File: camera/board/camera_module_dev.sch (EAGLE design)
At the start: 55 parts, among them IC1 74541PW, IC2 74541PW, Q1 MOSFET-NCHANNELBSS123LT1G, Q2 MOSFET-NCHANNELBSS123LT1G

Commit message: Fixed spacing for TCM camera pads, updated pullup resitor val on reset line
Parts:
- R5: value 10k -> 1k
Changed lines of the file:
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@@
 <part name="GND2" library="supply1" deviceset="GND" device=""/>
 <part name="GND3" library="supply1" deviceset="GND" device=""/>
-<part name="R5" library="biomimetic" deviceset="RESISTOR" device="0402-RES" value="10k"/>
+<part name="R5" library="biomimetic" deviceset="RESISTOR" device="0402-RES" value="1k"/>
 <part name="GND4" library="supply1" deviceset="GND" device=""/>
 <part name="GND5" library="supply1" deviceset="GND" device=""/>

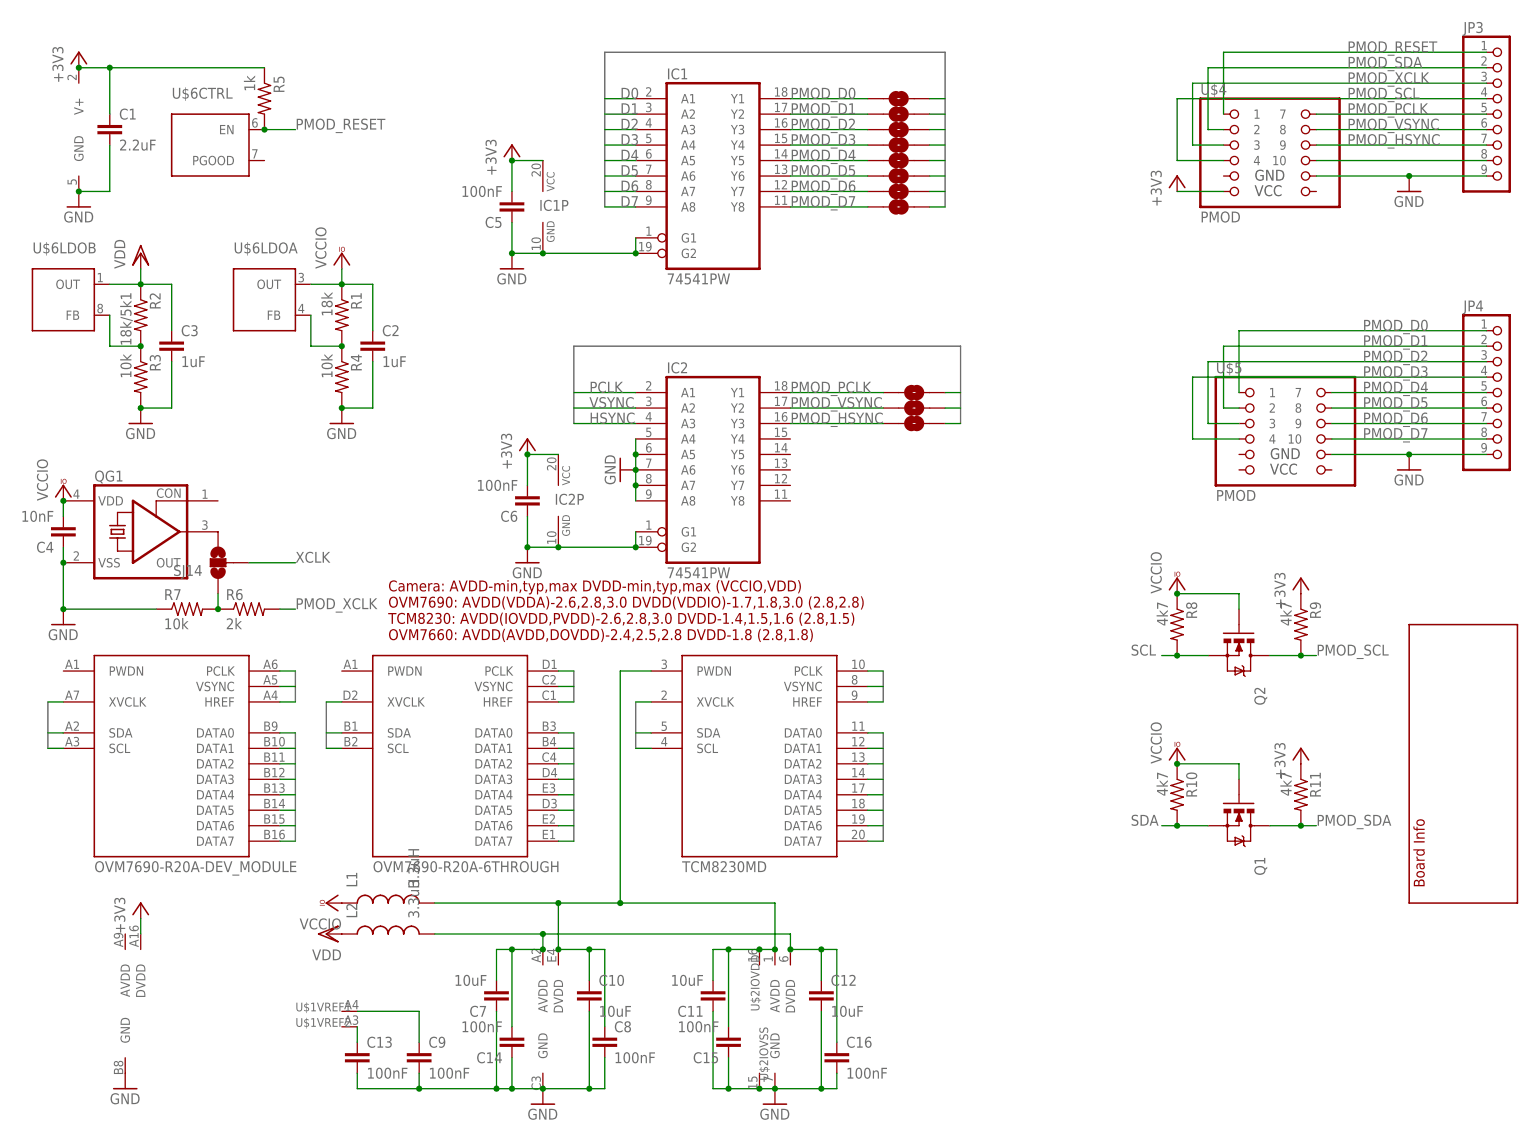
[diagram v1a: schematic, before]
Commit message: Laying out smaller TCM camera board
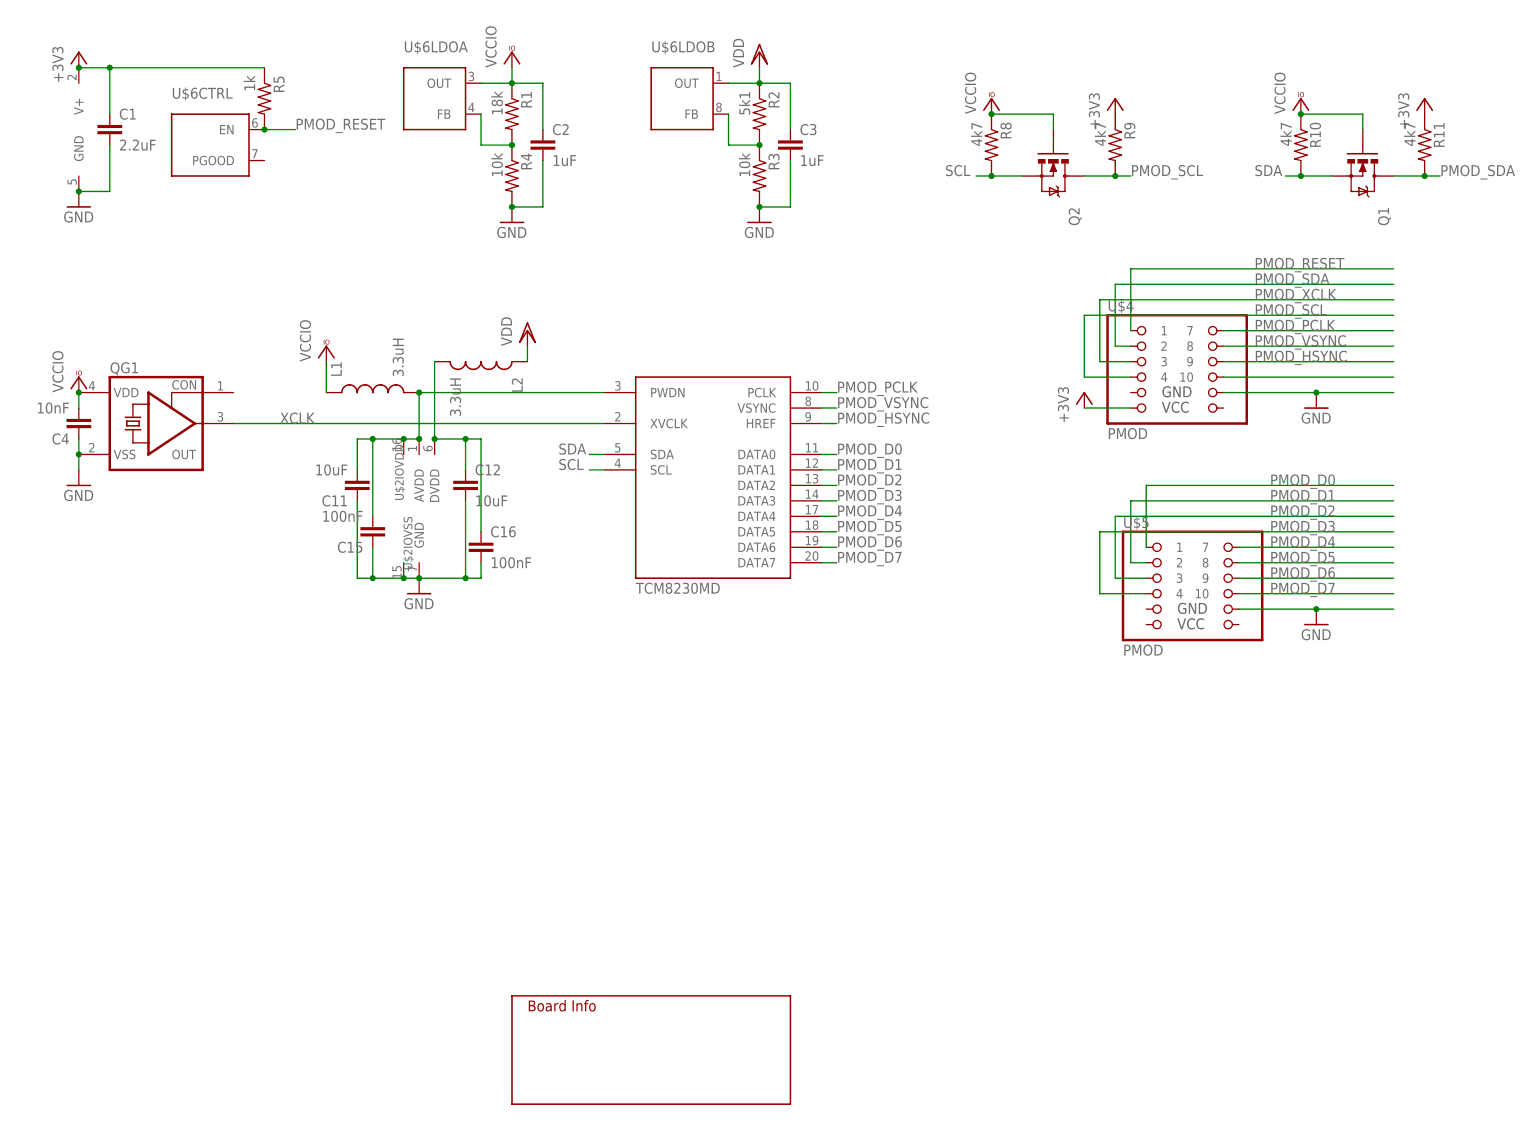
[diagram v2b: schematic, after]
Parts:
- removed C10, C7: 10uF, biomimetic:CAP0603-CAP
- removed C13, C14, C5, C6, C8, C9: 100nF, biomimetic:CAP0402-CAP
- removed IC1, IC2: 74541PW, modular_robotics:74541PW
- removed JP3, JP4: (no value), pinhead:PINHD-1X9
- removed R6: 2k, biomimetic:RESISTOR0402-RES
- removed R7: 10k, biomimetic:RESISTOR0402-RES
- removed SJ1, SJ10, SJ11, SJ2, SJ3, SJ4, SJ5, SJ6, SJ7, SJ8, SJ9: SOLDERJUMPERNO, SparkFun-Passives:SOLDERJUMPERNO
- removed SJ14: (no value), SparkFun-Passives:SOLDERJUMPER_2WAYS
- removed U$1: OVM7690-R20A-6THROUGH, modular_robotics:OVM7690-R20A-6THROUGH
- removed U$3: OVM7690-R20A-DEV_MODULE, modular_robotics:OVM7690-R20A-DEV_MODULE
- R2: value 18k/5k1 -> 5k1
- U$7: DATE Feb. 2014 -> Sep. 2014; DESIGN Dev Camera Module -> TCM8230 Camera Module; ORGANIZATION UC Berkeley Biomimetic Millisystems Lab -> UC Berkeley ASPIRE; REVISION r0.1 -> r1.0
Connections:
- removed net D0: IC1A.A1, SJ1.2, U$1G$1.DATA0, U$2G$1.DATA0, U$3G$1.DATA0
- removed net D1: IC1A.A2, SJ2.2, U$1G$1.DATA1, U$2G$1.DATA1, U$3G$1.DATA1
- removed net D2: IC1A.A3, SJ3.2, U$1G$1.DATA2, U$2G$1.DATA2, U$3G$1.DATA2
- removed net D3: IC1A.A4, SJ4.2, U$1G$1.DATA3, U$2G$1.DATA3, U$3G$1.DATA3
- removed net D4: IC1A.A5, SJ5.2, U$1G$1.DATA4, U$2G$1.DATA4, U$3G$1.DATA4
- removed net D5: IC1A.A6, SJ6.2, U$1G$1.DATA5, U$2G$1.DATA5, U$3G$1.DATA5
- removed net D6: IC1A.A7, SJ7.2, U$1G$1.DATA6, U$2G$1.DATA6, U$3G$1.DATA6
- removed net D7: IC1A.A8, SJ8.2, U$1G$1.DATA7, U$2G$1.DATA7, U$3G$1.DATA7
- removed net HSYNC: IC2A.A3, SJ11.2, U$1G$1.HREF, U$2G$1.HREF, U$3G$1.HREF
- removed net N$1: QG1.OUT, SJ14.3
- removed net N$3: R6.1, R7.2, SJ14.1
- removed net N$4: C13.1, U$1VREF2.V
- removed net N$5: C9.1, U$1VREF1.V
- removed net PCLK: IC2A.A1, SJ9.2, U$1G$1.PCLK, U$2G$1.PCLK, U$3G$1.PCLK
- removed net VSYNC: IC2A.A2, SJ10.2, U$1G$1.VSYNC, U$2G$1.VSYNC, U$3G$1.VSYNC
- net +3V3: no longer C5.2, C6.2, IC1P.VCC, IC2P.VCC, U$3G$2.DVDD
- net GND: no longer C10.2, C13.2, C14.1, C5.1, C6.1, C7.1, C8.2, C9.2, IC1A.G1, IC1A.G2, IC1P.GND, IC2A.A4, IC2A.A5, IC2A.A6, IC2A.A7, IC2A.A8, IC2A.G1, IC2A.G2, IC2P.GND, JP3.9, JP4.9, R7.1, U$1G$2.GND, U$3G$2.GND
- net N$2: no longer JP3.8
- net N$6: no longer C14.2, C7.2, U$1G$2.AVDD
- net N$8: no longer C10.1, C8.1, U$1G$2.DVDD
- net PMOD_D0: now also U$2G$1.DATA0; no longer IC1A.Y1, JP4.1, SJ1.1
- net PMOD_D1: now also U$2G$1.DATA1; no longer IC1A.Y2, JP4.2, SJ2.1
- net PMOD_D2: now also U$2G$1.DATA2; no longer IC1A.Y3, JP4.3, SJ3.1
- net PMOD_D3: now also U$2G$1.DATA3; no longer IC1A.Y4, JP4.4, SJ4.1
- net PMOD_D4: now also U$2G$1.DATA4; no longer IC1A.Y5, JP4.5, SJ5.1
- net PMOD_D5: now also U$2G$1.DATA5; no longer IC1A.Y6, JP4.6, SJ6.1
- net PMOD_D6: now also U$2G$1.DATA6; no longer IC1A.Y7, JP4.7, SJ7.1
- net PMOD_D7: now also U$2G$1.DATA7; no longer IC1A.Y8, JP4.8, SJ8.1
- net PMOD_HSYNC: now also U$2G$1.HREF; no longer IC2A.Y3, JP3.7, SJ11.1
- net PMOD_PCLK: now also U$2G$1.PCLK; no longer IC2A.Y1, JP3.5, SJ9.1
- net PMOD_RESET: no longer JP3.1
- net PMOD_SCL: no longer JP3.4
- net PMOD_SDA: no longer JP3.2
- net PMOD_VSYNC: now also U$2G$1.VSYNC; no longer IC2A.Y2, JP3.6, SJ10.1
- net PMOD_XCLK: no longer JP3.3, R6.2
- net SCL: no longer U$1G$1.SCL, U$3G$1.SCL
- net SDA: no longer U$1G$1.SDA, U$3G$1.SDA
- net XCLK: now also QG1.OUT; no longer SJ14.2, U$1G$1.XVCLK, U$3G$1.XVCLK
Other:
- note removed: "Camera: AVDD-min,typ,max DVDD-min,typ,max (VCCIO,VDD) OVM7690: AVDD(VDDA)-2.6,2.8,3.0 DVDD(VDDIO)-1.7,1.8,3.0 (2.8,2.8) TCM8230: AVDD(IOVDD,PVDD)-2.6,2.8,3.0 DVDD-1.4,1.5,1.6 (2.8,1.5) OVM7660: AVDD(AVDD,DOVDD)-2.4,2.5,2.8 DVDD-1.8 (2.8,1.8)"
- moved on the sheet: C11, C12, C15, C16, C2, C3, C4, L1, L2, Q1, Q2, QG1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

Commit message: Finished routing, silkscreen done, ready for panelization
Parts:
- U$7: AUTHOR Austin Buchan -> Austin Buchan (abuchan@berkeley.edu)
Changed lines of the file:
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@@
 </part>
 <part name="U$7" library="modular_robotics" deviceset="INFO" device="">
-<attribute name="AUTHOR" value="Austin Buchan"/>
+<attribute name="AUTHOR" value="Austin Buchan (abuchan@berkeley.edu)"/>
 <attribute name="DATE" value="Sep. 2014"/>
 <attribute name="DESIGN" value="TCM8230 Camera Module"/>
